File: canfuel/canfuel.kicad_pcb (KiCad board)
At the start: 2 copper layers, 55 x 45 mm, 28 parts, among them J1 Micro-Fit 43045-0400, J2 Micro-Fit 43045-0400, J3 ICSP, U1 PIC18F25K80, U2 MCP2562-E/P, Y1 16MHz

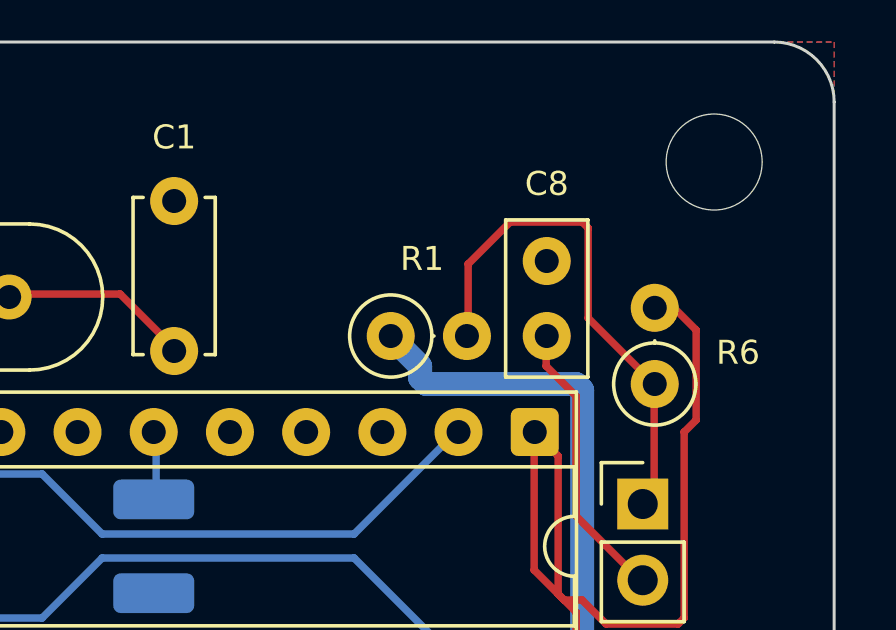
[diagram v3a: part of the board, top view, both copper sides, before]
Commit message: Move R1 1.20 mm clear of C8
R1 pad 2 and C8 pad 1 are MCLR_RC and MCLR_C - the two ends of JP2 - and
the search that placed the MCLR cluster left 1.06 mm of bare board between
them, with the courtyards touching at 0.03 mm. A solder bridge there would
hold the jumper closed for good, which is the one failure JP2 exists to
prevent, and the board would look fine until the first attempt to program
it.

Moving R1 west by 1.20 mm opens that gap to 2.26 mm. The move is sized by
the nearest-edge rule rather than by eye: R1 lands at 2.89 mm, inside the
3 mm assertion with a little margin, and costs about 0.9 mm of extra track
to the MCLR node - which R1, the 10k static pull-up, is the right part to
spend. ALLOW["2.3 R1"] goes 8.5 -> 9.0 to match, with the reason recorded
next to the number so a deliberate move and a regression still do not look
alike.

Two tracks were re-laid for it. +5V arrives on B.Cu along y = 61.4 and
used to step down into pad 1 exactly where pad 2 now sits, so the step
became a longer run west and one 45 degree diagonal; MCLR_RC gained a
45 degree diagonal from the new pad 2 up to the existing vertical at
x = 92.8. Pours refilled.

ERC, DRC, check-netlist.py and check-placement.py are all clean.

Also correct the netlist counts in CLAUDE.md and the plan to 87
connections and 24 components - 103 and 25 were from before J4 came off.

Co-Authored-By: Claude Opus 5 <noreply@anthropic.com>
Claude-Session: https://claude.ai/code/session_01Kv4qc9ux44VY2Vc2PTcGqV
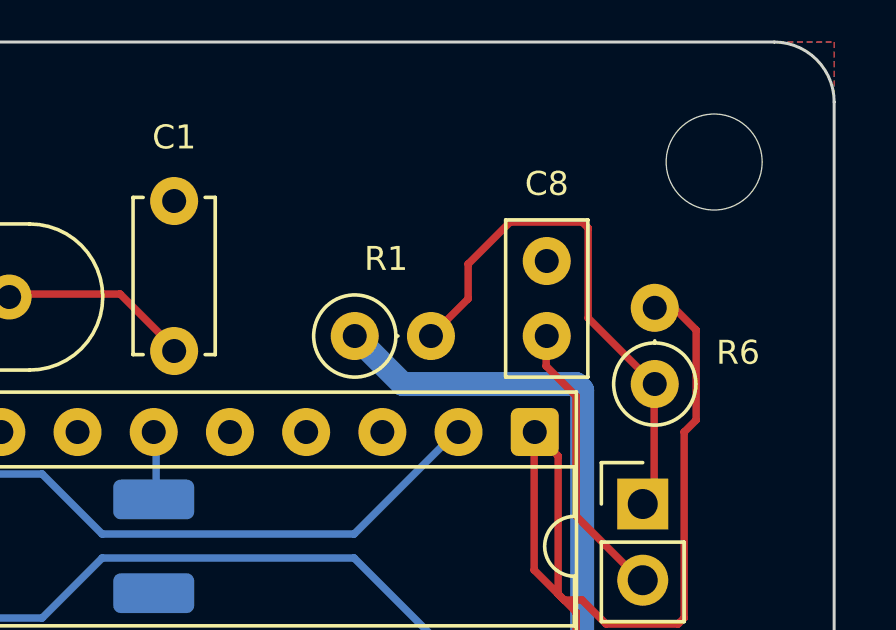
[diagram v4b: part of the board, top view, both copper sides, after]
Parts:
- moved R1 1.20 mm to (89.0, 59.8)
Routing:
- net +5V: track 164.8 -> 165.8 mm
- net MCLR_RC: track 17.3 -> 17.9 mm
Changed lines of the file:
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@@
 	(footprint "Resistor_THT:R_Axial_DIN0207_L6.3mm_D2.5mm_P2.54mm_Vertical"
 		(layer "F.Cu")
-		(at 90.22 59.8)
+		(at 89.02 59.8)
 		(descr "Resistor, Axial_DIN0207 series, Axial, Vertical, pin pitch=2.54mm, 0.25W = 1/4W, length*diameter=6.3*2.5mm^2, http://cdn-reichelt.de/documents/datenblatt/B400/1_4W%23YAG.pdf")
 		(tags "Resistor Axial_DIN0207 series Axial Vertical pin pitch 2.54mm 0.25W = 1/4W length 6.3mm diameter 2.5mm")
@@
 	)
 	(segment
-		(start 91.2 60.8)
-		(end 90.2 59.8)
-		(width 0.8)
-		(layer "B.Cu")
-		(net "+5V")
-	)
-	(segment
 		(start 96.4 61.4)
-		(end 91.4 61.4)
+		(end 90.62 61.4)
 		(width 0.8)
 		(layer "B.Cu")
@@
 	)
 	(segment
-		(start 91.4 61.4)
-		(end 91.2 61.2)
-		(width 0.8)
-		(layer "B.Cu")
-		(net "+5V")
-	)
-	(segment
 		(start 96.6 72)
 		(end 96.6 61.6)
@@
 	)
 	(segment
-		(start 91.2 61.2)
-		(end 91.2 60.8)
+		(start 90.62 61.4)
+		(end 89.02 59.8)
 		(width 0.8)
 		(layer "B.Cu")
@@
 	)
 	(segment
+		(start 91.56 59.8)
+		(end 92.8 58.56)
+		(width 0.25)
+		(layer "F.Cu")
+		(net "MCLR_RC")
+	)
+	(segment
 		(start 96.6 56)
 		(end 96.8 56.2)
@@
 	)
 	(segment
-		(start 92.8 59.8)
+		(start 92.8 58.56)
 		(end 92.8 57.4)
 		(width 0.25)

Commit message: Add canfuel fabrication outputs, and the 120R DNF legend they were missing
Plan section 6. canfuel/fab/ now holds nine gerbers, a merged Excellon drill
file, a drill map, a .gbrjob, the BOM and the CPL. The plan records the exact
commands: four of the kicad-cli defaults are wrong for this board, so the flags
are part of the design, not shell noise. --layers is required at all,
--check-zones stops a stale pour being what gets sent, --format csv --units mm
keeps export pos from writing an ASCII-in-inches file named .csv, and
--exclude-dnp keeps R5 out of the placement file.

The pre-order check in section 6 earned its keep. R5 is the 120 ohm
termination that must not be fitted, and the silkscreen legend saying so was
gone: moving value fields to F.Fab in the escape-header pass took it with them,
leaving the front silk reading "R5" and nothing else. Nothing else would have
caught it - ERC, DRC, check-netlist.py and check-placement.py are all
indifferent to silkscreen, and R5 has a footprint, pads and a value like any
other part. It is back as a board-level gr_text at (93.2, 91.5) rather than a
footprint field, so a future change to field placement cannot take it again.
DRC stays at zero violations with silk_overlap, silk_over_copper and
silk_edge_clearance all on.

.gitattributes said fab output must survive byte for byte and did not deliver
it: a pattern with a slash is anchored to the file's own directory, so fab/**
matched only a top-level fab/, never <board>/fab/. Now **/fab/**.

All four checks green before and after.

Co-Authored-By: Claude Opus 5 <noreply@anthropic.com>
Claude-Session: https://claude.ai/code/session_01ATgTvjD2bzuNhCtMT5joU9
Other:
- board text added: "120R DNF"
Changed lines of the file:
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@@
 		(layer "Edge.Cuts")
+	)
+	(gr_text "120R DNF"
+		(at 93.2 91.5 0)
+		(layer "F.SilkS")
+		(effects
+			(font
+				(size 0.8 0.8)
+				(thickness 0.12)
+			)
+		)
 	)
 	(segment
